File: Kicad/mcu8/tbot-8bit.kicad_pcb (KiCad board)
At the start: 2 copper layers, 80 x 100 mm, 60 parts, among them IC101 TLV1117-50, IC201 PIC16F1778, IC301 MCP2221A, K101 Battery, K201 MCU 1, K202 ICSP, K203 MCU 2, K301 FRONT #1, K302 FRONT #2, K303 VIN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

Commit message: Update
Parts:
- removed T101, T102: DMP2305U, tronixio:SOT-23-3
- added Q101: DIODESINC-DMP2305U-SOT-23, tronixio:SOT-23-3, F.Cu at (116.0, 137.0)
- added Q102: DIODESINC-DMP2305U-SOT-23, tronixio:SOT-23-3, F.Cu at (109.0, 137.0)
- IC101: value TLV1117-50 -> TI-TLV1117-50-SOT

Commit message: Update MCU
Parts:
- added TP103: KEYSTONE-2000-3, tronixio:KEYSTONE-2000-3, F.Cu at (194.0, 127.5)
- added TP104: KEYSTONE-2000-3, tronixio:KEYSTONE-2000-3, F.Cu at (197.2, 127.5)
- IC301: value MCP2221A -> MICROCHIP-MCP2221A-ISL
- TP101, TP102: value GND -> KEYSTONE-5006
- moved TP101 67.7 mm to (191.5, 134.0)
- moved TP102 12.0 mm to (188.0, 126.5)
- moved K202 1.50 mm to (106.5, 105.5)
- moved S201 1.50 mm to (108.0, 115.5)
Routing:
- net +5V: track 257.7 -> 254.9 mm
- net ~{MCLR}: track 27.6 -> 26.1 mm
- net Net-(C201-Pad1): track 18.3 -> 16.8 mm
- net /HID/RB7/PGD/URX: track 85.5 -> 84.0 mm
- net /HID/RB6/PGC/UTX: track 89.5 -> 88.0 mm
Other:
- board text added: "L"
- board text added: "R"

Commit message: Update tbot-8bit.kicad_pcb
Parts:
- added kibuzzard-62763CDA: G001, kibuzzard-62763CDA, F.Cu at (120.0, 57.0)
- added kibuzzard-62763CDA: G003, kibuzzard-62763CDA, F.Cu at (136.0, 57.0)
- added kibuzzard-62763CDA: G005, kibuzzard-62763CDA, F.Cu at (152.0, 57.0)
- added kibuzzard-62763D72: G006, kibuzzard-62763D72, F.Cu at (160.0, 57.0)
- added kibuzzard-62763D72: G002, kibuzzard-62763D72, F.Cu at (128.0, 57.0)
- added kibuzzard-62763D9F: G004, kibuzzard-62763D9F, F.Cu at (144.0, 57.0)
- added kibuzzard-62763E2E: G***, kibuzzard-62763E2E, F.Cu at (125.0, 143.0)
- added kibuzzard-62763E7E: G***, kibuzzard-62763E7E, F.Cu at (125.0, 141.0)

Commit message: Update tbot-8bit.kicad_pcb
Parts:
- removed the kibuzzard-62763CDA at (120.0, 57.0)
- removed kibuzzard-62763E2E: G***, kibuzzard-62763E2E
- added kibuzzard-62763E7E: G009, kibuzzard-62763E7E, F.Cu at (163.0, 99.0)
- added kibuzzard-62763E7E: G010, kibuzzard-62763E7E, F.Cu at (173.0, 126.0)
- added kibuzzard-62763E7E: G008, kibuzzard-62763E7E, F.Cu at (163.0, 109.5)
- added kibuzzard-6277F80B: G011, kibuzzard-6277F80B, F.Cu at (110.2, 77.5)
- added kibuzzard-6277F80B: G013, kibuzzard-6277F80B, F.Cu at (169.8, 77.5)
- added kibuzzard-6277F8A4: G012, kibuzzard-6277F8A4, F.Cu at (107.6, 77.5)
- added kibuzzard-6277F8A4: G014, kibuzzard-6277F8A4, F.Cu at (172.4, 77.5)
- added kibuzzard-6277F94E: G***, kibuzzard-6277F94E, F.Cu at (117.5, 131.5)
- added kibuzzard-6277F9C5: G001, kibuzzard-6277F9C5, F.Cu at (120.0, 56.9)
- kibuzzard-62763E7E: value G*** -> G007
- moved TP102 65.9 mm to (125.0, 146.0), turned to 90 degrees
- moved TP104 46.1 mm to (163.0, 96.5)
- moved TP103 34.7 mm to (163.0, 112.0)
- moved TP101 17.4 mm to (176.0, 126.0), turned to 0 degrees
- moved kibuzzard-62763E7E 2.00 mm to (125.0, 143.0)
- moved kibuzzard-62763CDA 0.10 mm to (136.0, 56.9)
- moved kibuzzard-62763CDA 0.10 mm to (152.0, 56.9)
- moved kibuzzard-62763D72 0.10 mm to (160.0, 56.9)
- moved kibuzzard-62763D72 0.10 mm to (128.0, 56.9)
- moved kibuzzard-62763D9F 0.10 mm to (144.0, 56.9)

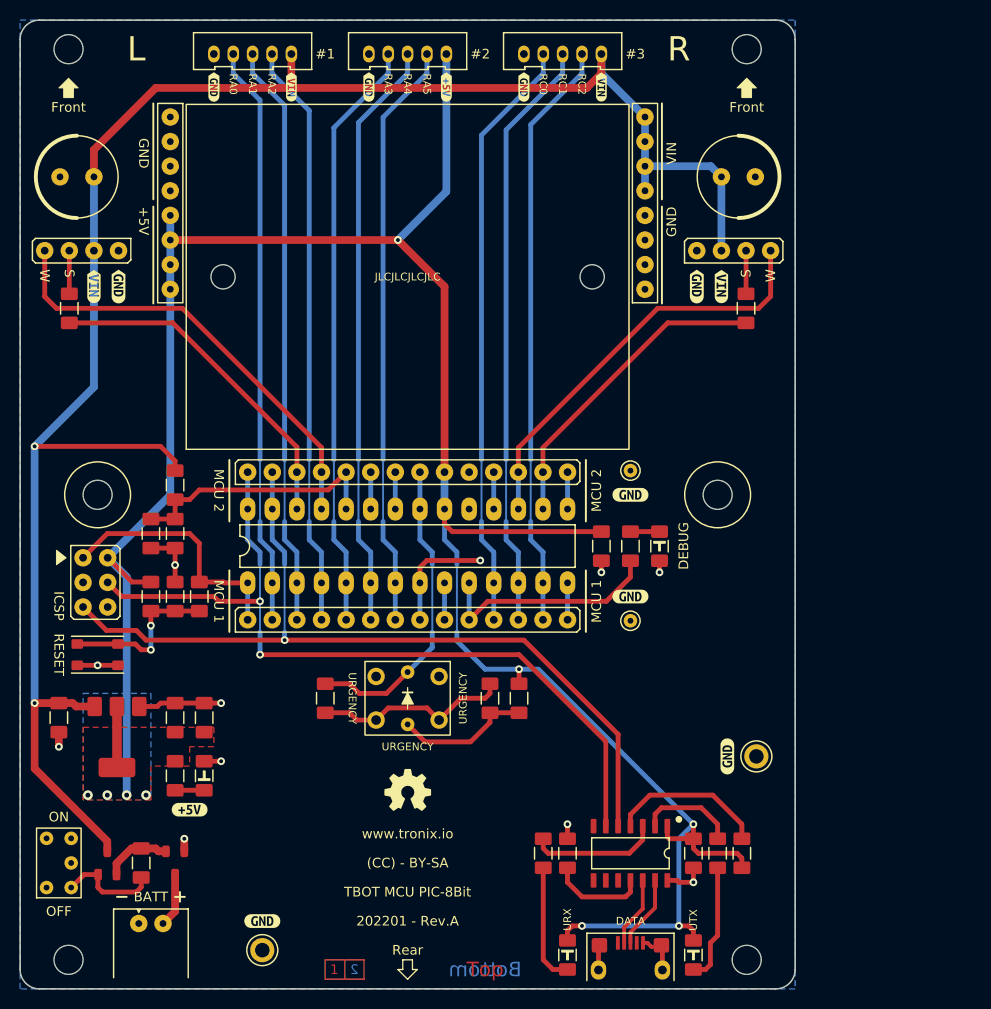
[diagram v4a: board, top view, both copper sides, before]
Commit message: Update MCU 8Bit
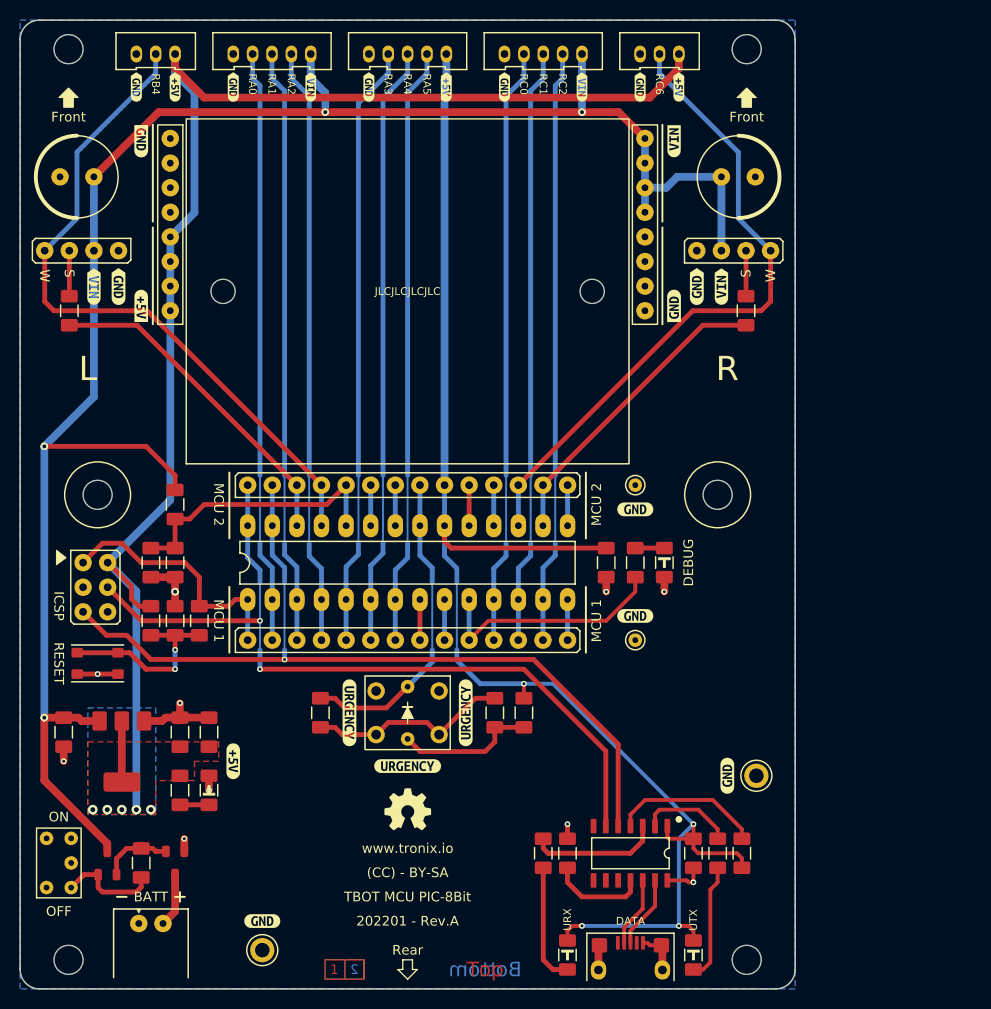
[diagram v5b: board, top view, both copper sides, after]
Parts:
- removed kibuzzard-6277F80B: G011, kibuzzard-6277F80B
- removed kibuzzard-6277F80B: G013, kibuzzard-6277F80B
- removed kibuzzard-6277F8A4: G012, kibuzzard-6277F8A4
- removed kibuzzard-6277F8A4: G014, kibuzzard-6277F8A4
- added K309: SERVO RIGHT, tronixio:HARWIN-M20-999044x, F.Cu at (169.8, 73.8)
- added K310: WHEEL RIGHT, tronixio:zzMOLEX-532530370, F.Cu at (164.0, 53.5)
- added kibuzzard-62763CDA: G003, kibuzzard-62763CDA, F.Cu at (164.0, 56.9)
- added kibuzzard-62763CDA: G003, kibuzzard-62763CDA, F.Cu at (112.0, 56.9)
- added kibuzzard-62763D9F: G004, kibuzzard-62763D9F, F.Cu at (116.0, 56.9)
- added kibuzzard-62763D9F: G004, kibuzzard-62763D9F, F.Cu at (168.0, 56.9)
- added kibuzzard-627FC68B: G***, kibuzzard-627FC68B, F.Cu at (172.4, 77.5)
- added kibuzzard-627FC691: G***, kibuzzard-627FC691, F.Cu at (169.8, 77.5)
- added kibuzzard-627FC699: G***, kibuzzard-627FC699, F.Cu at (107.6, 77.5)
- added kibuzzard-627FC69F: G***, kibuzzard-627FC69F, F.Cu at (110.2, 77.5)
- added kibuzzard-627FC6B4: G***, kibuzzard-627FC6B4, F.Cu at (146.0, 121.5)
- added kibuzzard-627FC6B4: G***, kibuzzard-627FC6B4, F.Cu at (134.0, 121.5)
- added kibuzzard-627FC6B4: G***, kibuzzard-627FC6B4, F.Cu at (140.0, 127.0)
- added kibuzzard-627FC8D5: G***, kibuzzard-627FC8D5, F.Cu at (167.5, 79.5)
- added kibuzzard-627FC905: G***, kibuzzard-627FC905, F.Cu at (167.5, 62.5)
- added kibuzzard-627FC965: G***, kibuzzard-627FC965, F.Cu at (112.5, 79.5)
- added kibuzzard-627FC987: G***, kibuzzard-627FC987, F.Cu at (112.5, 62.5)
- K307: value USB/UART -> WHEEL LEFT; footprint tronixio:FCI-USB-TYPE-B-MICRO-THT -> tronixio:zzMOLEX-532530370
- K308: value SERVO RIGHT -> USB/UART; footprint tronixio:HARWIN-M20-999044x -> tronixio:FCI-USB-TYPE-B-MICRO-THT
- moved K307 106.9 mm to (112.0, 53.5), turned to 0 degrees
- moved K308 74.0 mm to (163.0, 147.5)
- moved kibuzzard-6277F94E 6.73 mm to (122.0, 126.5), turned to -90 degrees
- moved C104 3.00 mm to (116.0, 106.0)
- moved R104 3.00 mm to (113.5, 106.0)
- moved C201 2.50 mm to (116.0, 112.0)
- moved R201 2.50 mm to (113.5, 112.0)
- moved R202 2.50 mm to (118.5, 112.0)
- moved K303 2.22 mm to (164.5, 62.2)
- moved K304 2.22 mm to (115.5, 80.0)
- moved K201 2.10 mm to (123.5, 114.0)
- moved TP103 2.06 mm to (163.5, 114.0)
- moved kibuzzard-62763E7E 2.06 mm to (163.5, 111.5)
- moved G*** 2.00 mm to (140.0, 131.5) (x2)
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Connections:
- K307 pad 1: unconnected-(K307-Pad1) -> +5V
- K307 pad 2: /HID/D- -> /HID/RB4/WHEEL_L
- K307 pad 3: /HID/D+ -> GND
- K308 pad 1: GND -> unconnected-(K308-Pad1)
- K308 pad 2: VIN -> /HID/D-
- K308 pad 3: Net-(K308-Pad3) -> /HID/D+
- K308 pad 4: /HID/RC6/WHEEL_R -> unconnected-(K308-Pad4)
- R308 pad 2: Net-(K308-Pad3) -> Net-(K309-Pad3)
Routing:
- net +5V: track 254.9 -> 308.7 mm, vias 9 -> 10
- net /HID/RC6/WHEEL_R: track 43.6 -> 68.4 mm
- net /HID/RB4/WHEEL_L: track 46.1 -> 70.9 mm
- net Net-(K309-Pad3): track 0.00 -> 4.70 mm
- net Net-(K308-Pad3): track 4.45 -> 0.00 mm
- net GND: track 50.1 -> 46.4 mm, vias 11 -> 10
- net Net-(C201-Pad1): track 16.8 -> 19.3 mm
- net RB3/BATTERY_SENSE: track 27.1 -> 28.8 mm
- net /HID/RA1: track 60.3 -> 61.6 mm
- net /HID/RA2: track 60.5 -> 61.8 mm
- net /HID/RA0: track 60.1 -> 61.3 mm
- net /HID/RA4: track 61.0 -> 62.1 mm
- net /HID/RA5: track 60.8 -> 61.9 mm
- net /HID/RA3: track 61.2 -> 62.3 mm
- net /HID/RA6/LED: track 24.0 -> 24.9 mm
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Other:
- board text added: "RB4"
- board text added: "RC6"
- board text removed: "#1"
- board text removed: "#2"
- board text removed: "#3"
- board text removed: "URGENCY"

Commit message: Update MCU 8Bit
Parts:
- K307: value WHEEL LEFT -> LEFT
- K310: value WHEEL RIGHT -> RIGHT
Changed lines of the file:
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@@
       (effects (font (size 1 1) (thickness 0.15)))
     )
-    (fp_text value "WHEEL LEFT" (at 2 3) (layer "F.Fab")
+    (fp_text value "LEFT" (at 2 3) (layer "F.Fab")
       (effects (font (size 1 1) (thickness 0.15)))
     )
@@
       (effects (font (size 1 1) (thickness 0.15)))
     )
-    (fp_text value "WHEEL RIGHT" (at 2 3) (layer "F.Fab")
-      (effects (font (size 1 1) (thickness 0.15)))
-    )
+    (fp_text value "RIGHT" (at 2 3) (layer "F.Fab")
+      (effects (font (size 1 1) (thickness 0.15)))
+    )

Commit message: Update
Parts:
- S301: value EMERGENCY -> URGENCY; footprint tronixio:E-SWITCH-TL1240XQ1JXXX -> tronixio:zzzOMRON-B3W9000-X1
- moved kibuzzard-627FC6B4 1.50 mm to (140.0, 128.5)
- moved G*** 1.00 mm to (140.0, 132.5) (x2)
- moved kibuzzard-627FC6B4 0.71 mm to (146.5, 122.0)
- moved kibuzzard-627FC6B4 0.71 mm to (133.5, 122.0)
- moved S301 0.50 mm to (140.0, 122.0), turned to 90 degrees
- turned R301 to -90 degrees
- turned R302 to 90 degrees
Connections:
- net /HID/RB0/EMERGENCY renamed /HID/RB0/URGENCY
- S301 pad 1: GND -> Net-(R302-Pad1)
- S301 pad 2: GND -> Net-(R302-Pad1)
- S301 pad 3: Net-(R302-Pad1) -> GND
- S301 pad 4: Net-(R302-Pad1) -> GND
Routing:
- net Net-(R301-Pad1): track 14.5 -> 16.4 mm
- net Net-(R302-Pad1): track 20.9 -> 19.0 mm
- net +5V: track 308.7 -> 310.0 mm

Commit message: Update
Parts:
- added Q301: DIODESINC-DMP2305U-SOT-23, tronixio:SOT-23-3, F.Cu at (112.5, 88.5)
- added Q302: DIODESINC-DMP2305U-SOT-23, tronixio:SOT-23-3, F.Cu at (167.5, 88.5)
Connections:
- net RC7 renamed /HID/RC7/WHEEL_R_EN
- C104 pad 1: RB3/BATTERY_SENSE -> RB2/BATTERY_SENSE
- IC201 pad 23: RB2 -> RB2/BATTERY_SENSE
- IC201 pad 24: RB3/BATTERY_SENSE -> /HID/RB3/WHEEL_L_EN
- K203 pad 5: RB3/BATTERY_SENSE -> /HID/RB3/WHEEL_L_EN
- K203 pad 6: RB2 -> RB2/BATTERY_SENSE
- K307 pad 1: +5V -> Net-(K307-Pad1)
- K310 pad 1: +5V -> Net-(K310-Pad1)
- R103 pad 1: RB3/BATTERY_SENSE -> RB2/BATTERY_SENSE
- R104 pad 2: RB3/BATTERY_SENSE -> RB2/BATTERY_SENSE
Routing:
- net Net-(K307-Pad1): track 0.00 -> 35.2 mm, vias 0 -> 1
- net Net-(K310-Pad1): track 0.00 -> 34.0 mm, vias 0 -> 1
- net /HID/RB3/WHEEL_L_EN: track 0.00 -> 32.0 mm
- net RB2/BATTERY_SENSE: track 0.00 -> 31.8 mm
- net +5V: track 310.0 -> 280.2 mm, vias 10 -> 11
- net RB3/BATTERY_SENSE: track 28.8 -> 0.00 mm
- net /HID/RC7/WHEEL_R_EN: track 4.19 -> 28.3 mm
- net RB2: track 4.19 -> 0.00 mm
- net GND: track 46.4 -> 47.5 mm
